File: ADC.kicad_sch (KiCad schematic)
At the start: 32 parts, among them U107 ADR4540, U111 ADA4841-1, U97 AD7768

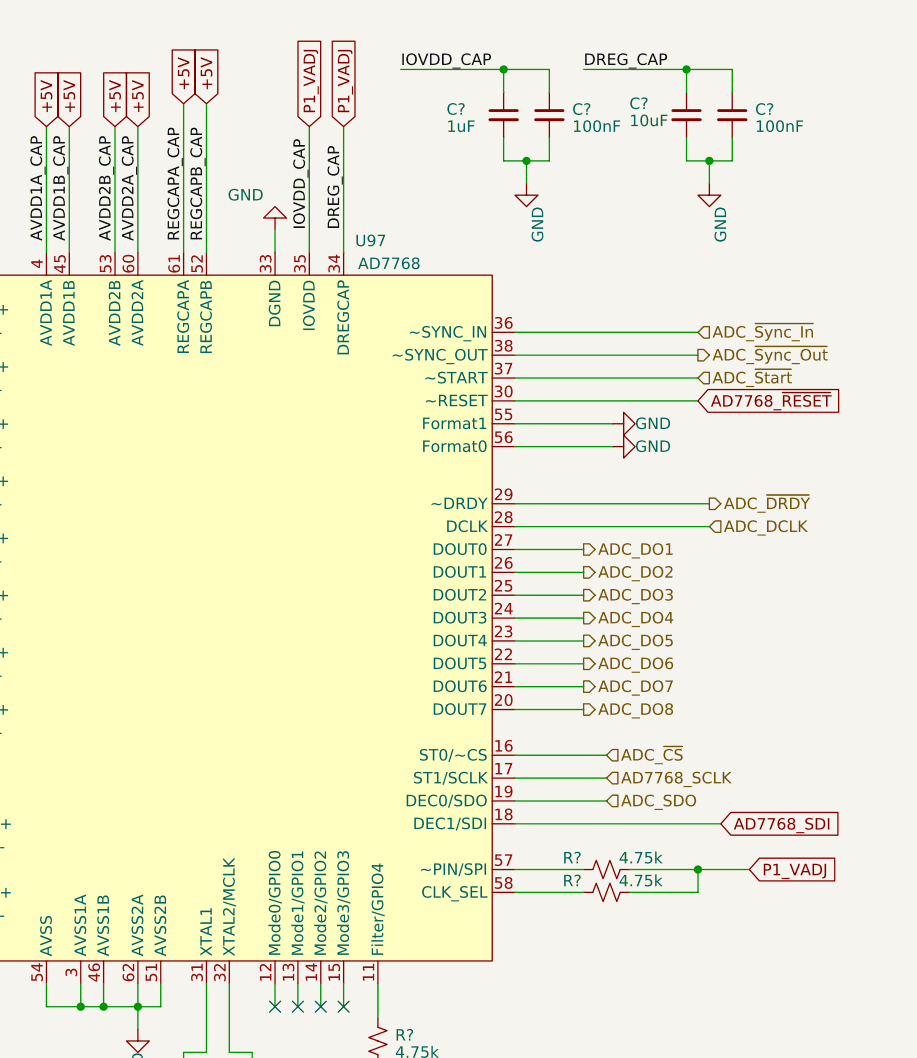
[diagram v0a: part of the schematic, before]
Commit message: Completed Schmatic and Layout
All Schematic and Layout Task are complete with the following exceptions:
- Adjust Silkscreen Layers
- Add Osprey Logo and Serial Number

Note-Removed Files no longer reference in the project
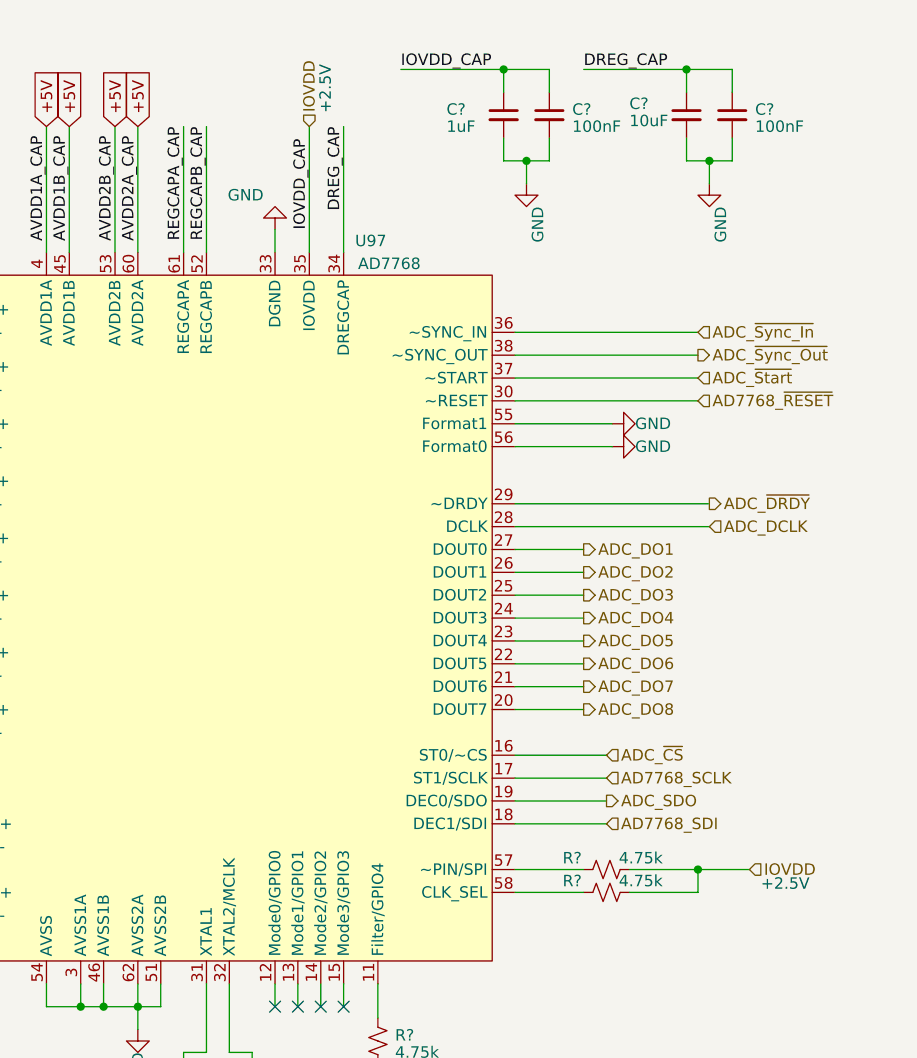
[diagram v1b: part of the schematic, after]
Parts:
- removed C? (x13): 100nF, Capacitor_SMD:C_0402_1005Metric, symbol Device:C_Small
- removed C?: 10uF, Capacitor_SMD:C_0805_2012Metric, symbol Device:C_Small
- removed C? (x9): 1uF, Capacitor_SMD:C_0402_1005Metric, symbol Device:C_Small
- removed C?: 47nF, Capacitor_SMD:C_0402_1005Metric, symbol Device:C_Small
- removed R?: 100R, Resistor_SMD:R_0402_1005Metric, symbol Device:R_Small_US
- removed R? (x3): 4.75k, Resistor_SMD:R_0402_1005Metric, symbol Device:R_Small_US
- removed R?: 49R9, Resistor_SMD:R_0402_1005Metric, symbol Device:R_Small_US
- added C? (x13): 100nF, Capacitor_SMD:C_0402_1005Metric, symbol Device:C_Small
- added C?: 10uF, Capacitor_SMD:C_0805_2012Metric, symbol Device:C_Small
- added C? (x9): 1uF, Capacitor_SMD:C_0402_1005Metric, symbol Device:C_Small
- added C?: 47nF, Capacitor_SMD:C_0402_1005Metric, symbol Device:C_Small
- added R? (x3): 4.75k, Resistor_SMD:R_0402_1005Metric, symbol Device:R_Small_US
- added R?: 49R9, Resistor_SMD:R_0402_1005Metric, symbol Device:R_Small_US
- added R?: 100R, Resistor_SMD:R_0402_1005Metric, symbol Device:R_Small_US
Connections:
- net +5V: now also C?.1, C?.1, C?.1, C?.1, C?.1, C?.1, C?.1, C?.1, C?.1, C?.1; no longer U97.52 (REGCAPB), U97.61 (REGCAPA)
- net ADC_MCLK+: now also C?.2
- net ADC_MCLK-: now also C?.2
- net ADC_VCM: now also C?.1, R?.1
- net GND: now also C?.1, C?.1, C?.2, C?.2, C?.2, C?.2, C?.2, C?.2, C?.2, C?.2, C?.2, C?.2, C?.2, C?.2, C?.2, C?.2, C?.2, C?.2, C?.2, C?.2, C?.2, C?.2, R?.2
- net at U97.31 (XTAL1): now also C?.1, R?.1
- net at U97.32 (XTAL2/MCLK): now also C?.1, R?.2
- net at U97.58 (CLK_SEL): now also R?.2
- net at U97.11 (Filter/GPIO4): now also R?.1
- net at U111.1, U111.4 (-), U97.43 (REF2+)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: now also C?.2, C?.2
- net at U97.57 (~PIN/SPI): now also R?.2
- net at U97.59 (VCM): now also R?.2
- net at U107.6 (OUT), U111.3 (+): now also C?.1
- net P1_VADJ renamed DREG_CAP
- net DREG_CAP: now also C?.1, C?.1; no longer U97.35 (IOVDD)
- new net IOVDD: C?.1, C?.1, R?.1, R?.1, U97.35 (IOVDD)
- new net REGCAPA_CAP: C?.1, C?.1, U97.61 (REGCAPA)
- new net REGCAPB_CAP: C?.1, C?.1, U97.52 (REGCAPB)
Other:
- note added: "+2.5V"

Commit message: Updated PCB
Adjusted Silkscreen
Added Logo and SN location
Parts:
- C? (x13): MPN CL10B104KB8NNWC -> CL05A104KA5NNNC
- C? (x7): MPN CC0603KRX7R7BB105 -> CL05X105KP5NNNC
- C? (x2): MPN (none) -> CL05X105KP5NNNC
- C?: MPN (none) -> GRT155R61C474KE01D
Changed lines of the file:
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@@
       (effects (font (size 1.27 1.27)) hide)
     )
-    (property "MPN" "CL10B104KB8NNWC" (at 213.995 31.75 0)
+    (property "MPN" "CL05A104KA5NNNC" (at 213.995 31.75 0)
       (effects (font (size 1.27 1.27)) hide)
     )
@@
       (effects (font (size 1.27 1.27)) hide)
     )
-    (property "MPN" "CL10B104KB8NNWC" (at 85.725 31.75 0)
+    (property "MPN" "CL05A104KA5NNNC" (at 85.725 31.75 0)
       (effects (font (size 1.27 1.27)) hide)
     )
@@
       (effects (font (size 1.27 1.27)) hide)
     )
-    (property "MPN" "CC0603KRX7R7BB105" (at 60.325 54.61 0)
+    (property "MPN" "CL05X105KP5NNNC" (at 60.325 54.61 0)
       (effects (font (size 1.27 1.27)) hide)
     )
@@
       (effects (font (size 1.27 1.27)) hide)
     )
-    (property "MPN" "CC0603KRX7R7BB105" (at 100.965 31.75 0)
+    (property "MPN" "CL05X105KP5NNNC" (at 100.965 31.75 0)
       (effects (font (size 1.27 1.27)) hide)
     )
@@
       (effects (font (size 1.27 1.27)) hide)
     )
-    (property "MPN" "" (at 130.175 120.65 0)
+    (property "MPN" "CL05X105KP5NNNC" (at 130.175 120.65 0)
       (effects (font (size 1.27 1.27)) hide)
     )
@@
       (effects (font (size 1.27 1.27)) hide)
     )
-    (property "MPN" "CL10B104KB8NNWC" (at 107.315 54.61 0)
+    (property "MPN" "CL05A104KA5NNNC" (at 107.315 54.61 0)
       (effects (font (size 1.27 1.27)) hide)
     )
@@
       (effects (font (size 1.27 1.27)) hide)
     )
-    (property "MPN" "CC0603KRX7R7BB105" (at 81.915 54.61 0)
+    (property "MPN" "CL05X105KP5NNNC" (at 81.915 54.61 0)
       (effects (font (size 1.27 1.27)) hide)
     )
@@
       (effects (font (size 1.27 1.27)) hide)
     )
-    (property "MPN" "CL10B104KB8NNWC" (at 180.975 144.78 0)
+    (property "MPN" "CL05A104KA5NNNC" (at 180.975 144.78 0)
       (effects (font (size 1.27 1.27)) hide)
     )
@@
       (effects (font (size 1.27 1.27)) hide)
     )
-    (property "MPN" "CL10B104KB8NNWC" (at 89.535 120.65 0)
+    (property "MPN" "CL05A104KA5NNNC" (at 89.535 120.65 0)
       (effects (font (size 1.27 1.27)) hide)
     )
@@
       (effects (font (size 1.27 1.27)) hide)
     )
-    (property "MPN" "CL10B104KB8NNWC" (at 234.315 31.75 0)
+    (property "MPN" "CL05A104KA5NNNC" (at 234.315 31.75 0)
       (effects (font (size 1.27 1.27)) hide)
     )
@@
       (effects (font (size 1.27 1.27)) hide)
     )
-    (property "MPN" "CC0603KRX7R7BB105" (at 102.235 54.61 0)
+    (property "MPN" "CL05X105KP5NNNC" (at 102.235 54.61 0)
       (effects (font (size 1.27 1.27)) hide)
     )
@@
       (effects (font (size 1.27 1.27)) hide)
     )
-    (property "MPN" "CL10B104KB8NNWC" (at 94.615 107.95 0)
+    (property "MPN" "CL05A104KA5NNNC" (at 94.615 107.95 0)
       (effects (font (size 1.27 1.27)) hide)
     )
@@
       (effects (font (size 1.27 1.27)) hide)
     )
-    (property "MPN" "CC0603KRX7R7BB105" (at 80.645 31.75 0)
+    (property "MPN" "CL05X105KP5NNNC" (at 80.645 31.75 0)
       (effects (font (size 1.27 1.27)) hide)
     )
@@
       (effects (font (size 1.27 1.27)) hide)
     )
-    (property "MPN" "CL10B104KB8NNWC" (at 69.215 111.76 0)
+    (property "MPN" "CL05A104KA5NNNC" (at 69.215 111.76 0)
       (effects (font (size 1.27 1.27)) hide)
     )
@@
       (effects (font (size 1.27 1.27)) hide)
     )
-    (property "MPN" "CC0603KRX7R7BB105" (at 60.325 31.75 0)
+    (property "MPN" "CL05X105KP5NNNC" (at 60.325 31.75 0)
       (effects (font (size 1.27 1.27)) hide)
     )
@@
       (effects (font (size 1.27 1.27)) hide)
     )
-    (property "MPN" "CC0603KRX7R7BB105" (at 208.915 31.75 0)
+    (property "MPN" "CL05X105KP5NNNC" (at 208.915 31.75 0)
       (effects (font (size 1.27 1.27)) hide)
     )
@@
       (effects (font (size 1.27 1.27)) hide)
     )
-    (property "MPN" "CL10B104KB8NNWC" (at 173.355 144.78 0)
+    (property "MPN" "CL05A104KA5NNNC" (at 173.355 144.78 0)
       (effects (font (size 1.27 1.27)) hide)
     )
@@
       (effects (font (size 1.27 1.27)) hide)
     )
-    (property "MPN" "CL10B104KB8NNWC" (at 65.405 54.61 0)
+    (property "MPN" "CL05A104KA5NNNC" (at 65.405 54.61 0)
       (effects (font (size 1.27 1.27)) hide)
     )
@@
       (effects (font (size 1.27 1.27)) hide)
     )
-    (property "MPN" "CL10B104KB8NNWC" (at 65.405 31.75 0)
+    (property "MPN" "CL05A104KA5NNNC" (at 65.405 31.75 0)
       (effects (font (size 1.27 1.27)) hide)
     )
@@
       (effects (font (size 1.27 1.27)) hide)
     )
-    (property "MPN" "CL10B104KB8NNWC" (at 86.995 54.61 0)
+    (property "MPN" "CL05A104KA5NNNC" (at 86.995 54.61 0)
       (effects (font (size 1.27 1.27)) hide)
     )
@@
       (effects (font (size 1.27 1.27)) hide)
     )
-    (property "MPN" "" (at 126.365 99.06 0)
+    (property "MPN" "GRT155R61C474KE01D" (at 126.365 99.06 0)
       (effects (font (size 1.27 1.27)) hide)
     )
@@
       (effects (font (size 1.27 1.27)) hide)
     )
-    (property "MPN" "CL10B104KB8NNWC" (at 106.045 31.75 0)
+    (property "MPN" "CL05A104KA5NNNC" (at 106.045 31.75 0)
       (effects (font (size 1.27 1.27)) hide)
     )
@@
       (effects (font (size 1.27 1.27)) hide)
     )
-    (property "MPN" "" (at 130.175 113.03 0)
-      (effects (font (size 1.27 1.27)) hide)
-    )
+    (property "MPN" "CL05X105KP5NNNC" (at 130.175 113.03 0)
+      (effects (font (size 1.27 1.27)) hide)
+    )

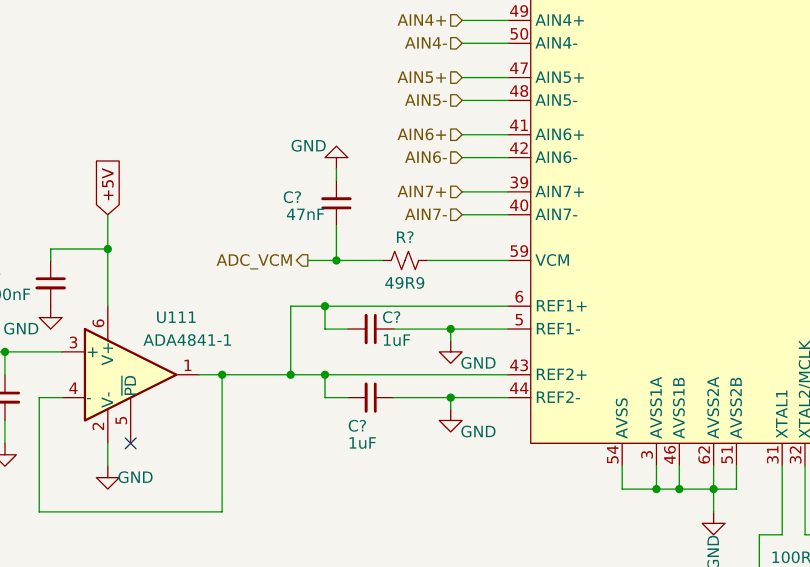
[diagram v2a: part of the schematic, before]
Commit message: Finalized Design & Board
Change to design
-Added resistor options to choose the grounding of input connectors
-uploaded libraries
-uploaded generated BOM
- adjusted mounting holes on front of board by 10mil
-Changed input AC blocking cap to 10nF from 100nF due to part availability
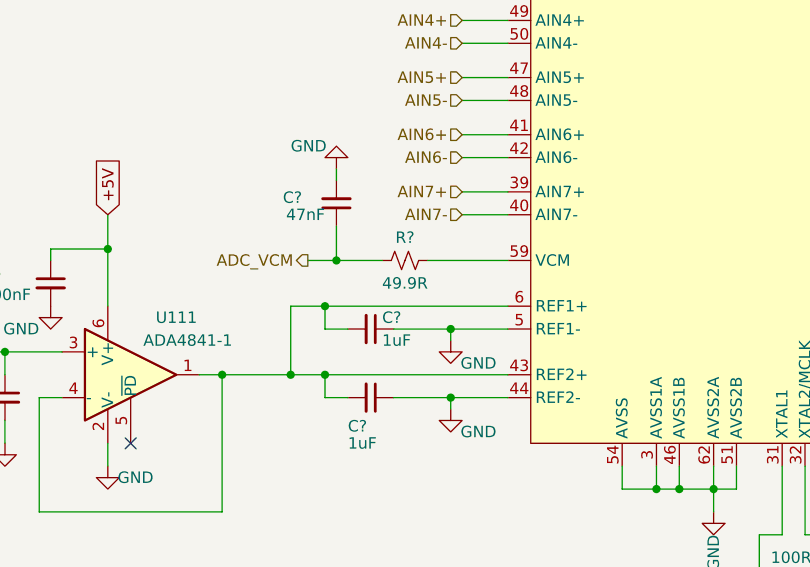
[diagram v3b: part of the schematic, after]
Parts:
- R? (x2): MPN RC0603FR-074K75L -> RC0402FR-074K75L
- R?: MPN (none) -> RC0402FR-074K75L
- R?: value 49R9 -> 49.9R; MPN RT0603FRE0749R9L -> RC0402FR-0749R9L
- R?: MPN (none) -> RC0402FR-07100RL
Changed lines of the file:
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@@
       (effects (font (size 1.27 1.27)) hide)
     )
-    (property "MPN" "RC0603FR-074K75L" (at 220.345 115.57 90)
+    (property "MPN" "RC0402FR-074K75L" (at 220.345 115.57 90)
       (effects (font (size 1.27 1.27)) hide)
     )
@@
       (effects (font (size 1.27 1.27)) hide)
     )
+    (property "MPN" "RC0402FR-074K75L" (at 194.945 134.62 0)
+      (effects (font (size 1.27 1.27)) hide)
+    )
     (pin "1")
     (pin "2")
@@
       (effects (font (size 1.27 1.27)))
     )
-    (property "Value" "49R9" (at 133.985 107.95 90)
+    (property "Value" "49.9R" (at 133.985 107.95 90)
       (effects (font (size 1.27 1.27)))
     )
@@
       (effects (font (size 1.27 1.27)) hide)
     )
-    (property "MPN" "RT0603FRE0749R9L" (at 133.985 105.41 90)
+    (property "MPN" "RC0402FR-0749R9L" (at 133.985 105.41 90)
       (effects (font (size 1.27 1.27)) hide)
     )
@@
       (effects (font (size 1.27 1.27)) hide)
     )
-    (property "MPN" "" (at 177.165 140.97 90)
+    (property "MPN" "RC0402FR-07100RL" (at 177.165 140.97 90)
       (effects (font (size 1.27 1.27)) hide)
     )
@@
       (effects (font (size 1.27 1.27)) hide)
     )
-    (property "MPN" "RC0603FR-074K75L" (at 220.345 118.11 90)
-      (effects (font (size 1.27 1.27)) hide)
-    )
+    (property "MPN" "RC0402FR-074K75L" (at 220.345 118.11 90)
+      (effects (font (size 1.27 1.27)) hide)
+    )

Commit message: Updated to version 1.2.1
This update fixes a few production documentation issues.
The boards will be functionally identical to v1.2.
With this update and going forward I moved away from version number as a part of filenames

Updates:
BOM ITEM 3 GRT155R61C474KE01D -> CGA2B3X7R1H473K050BB (wrong value)
BOM ITEM 7 GRM1885C1H101JA01D -> GRM1555C1H101JA01D (wrong size)

Corrected MPN description on BOM items 1&3 (CL05X105KP5NNNC &CL21A106KOQNNNE)

Updated Silkscreen with Version Number
Updated Schematic Title Block with current Date and Version Number
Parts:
- C?: MPN GRT155R61C474KE01D -> CGA2B3X7R1H473K050BB
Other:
- company: (none) -> OspreyDCS
- title: (none) -> Quartz
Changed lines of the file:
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@@
 (kicad_sch (version 20230121) (generator eeschema)
   (paper "A4")
+  (title_block
+    (title "Quartz")
+    (date "2024-03-28")
+    (rev "v1.2.1")
+    (company "OspreyDCS")
+  )
   (junction (at 60.325 26.67) (diameter 0) (color 0 0 0 0)
   )
@@
       (effects (font (size 1.27 1.27)) hide)
     )
-    (property "MPN" "GRT155R61C474KE01D" (at 126.365 99.06 0)
+    (property "MPN" "CGA2B3X7R1H473K050BB" (at 126.365 99.06 0)
       (effects (font (size 1.27 1.27)) hide)
     )
